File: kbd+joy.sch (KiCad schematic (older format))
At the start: 50 parts, among them CN2 KEYBOARD_HEADER, CN4 JOY1, CN5 JOY2, U11 74LS125, U13 MOS_6529

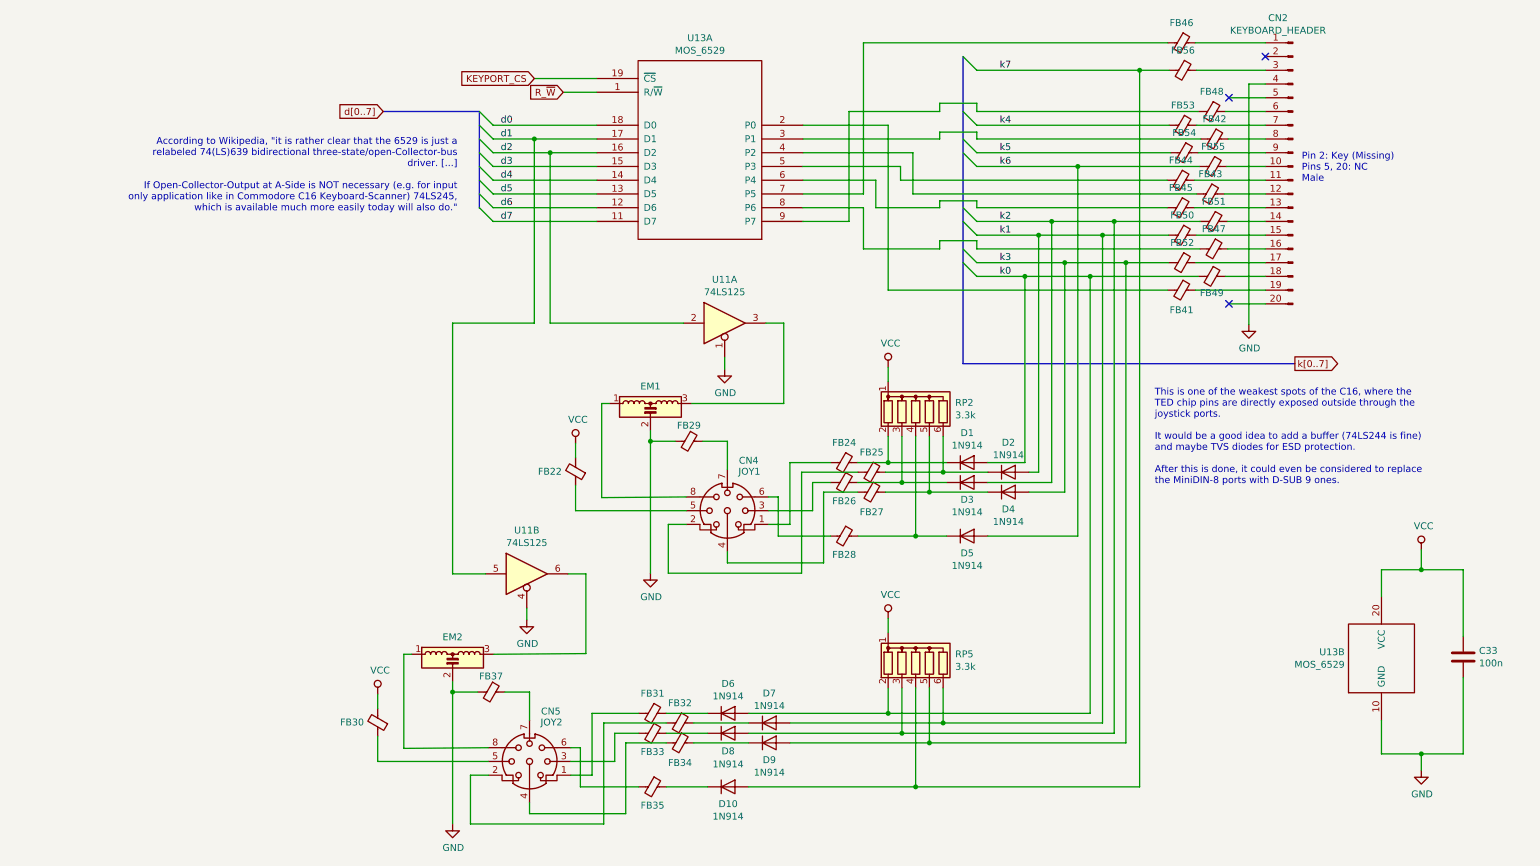
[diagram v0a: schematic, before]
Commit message: Map RP3/4 and add (J)D1/2
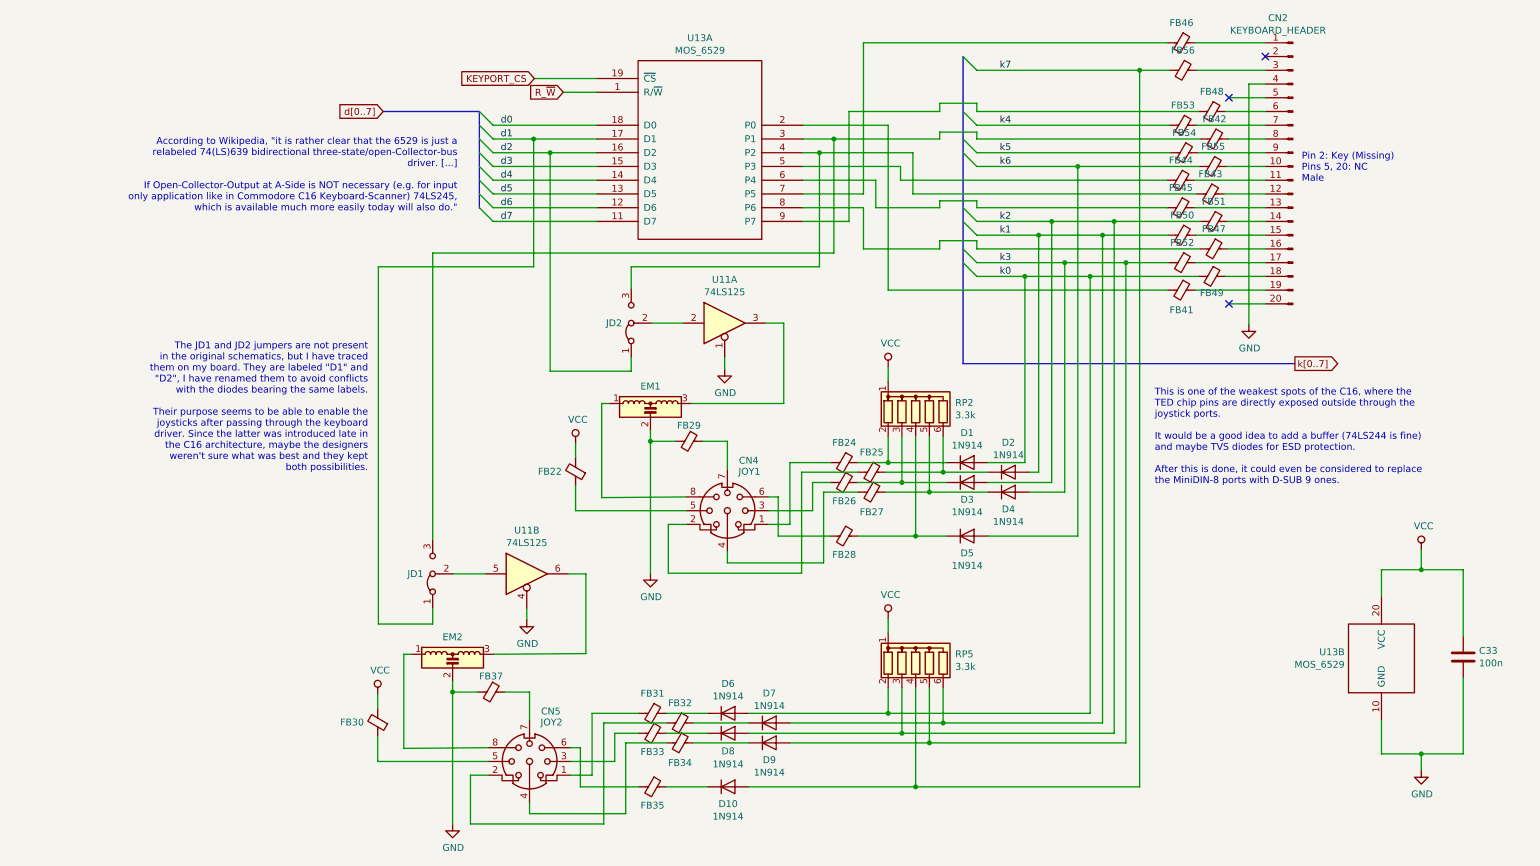
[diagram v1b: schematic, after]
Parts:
- added JD1, JD2: Jumper_3_Bridged12, LittleSixteen:SolderJumper2x, symbol Jumper:Jumper_3_Bridged12
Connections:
- net d1: now also JD1.1 (A); no longer U11.5
- net d2: now also JD2.1 (A); no longer U11.2
- net at FB42.2, U13.3 (P1): now also JD1.3 (B)
- net at FB43.2, U13.4 (P2): now also JD2.3 (B)
- new net: JD2.2 (C), U11.2
- new net: JD1.2 (C), U11.5
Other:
- note added: "The JD1 and JD2 jumpers are not present\nin the original schematics, but I have traced\nthem on my board. They are labeled "D1" and\n"D2", I have renamed them to avoid conflicts\nwith the diodes bearing the same labels.\n\nTheir purpose seems to be able to enable the\njoysticks after passing through the keyboard\ndriver. Since the latter was introduced late in\nthe C16 architecture, maybe the des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"
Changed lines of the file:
@@
 Sheet 6 11
 Title "LittleSixteen"
-Date "2020-01-03"
+Date "2020-01-20"
 Rev "1git"
 Comp "SukkoPera"
@@
 	6485 1480 6485 2680
 Wire Wire Line
-	5865 1680 6665 1680
+	5865 1680 5985 1680
 Wire Wire Line
 	6665 1680 6665 1980
@@
 	7030 1580 7130 1680
 Wire Wire Line
-	5865 1580 6860 1580
+	5865 1580 6090 1580
 Wire Wire Line
 	6860 1580 6860 1530
@@
 	4365 1480 3610 1480
 Wire Wire Line
-	4365 1580 3910 1580
+	4365 1580 3905 1580
 Wire Wire Line
 	4365 1680 4025 1680
@@
 Wire Wire Line
 	5295 3255 5295 3170
-Wire Wire Line
-	4025 1680 4025 2920
-Wire Wire Line
-	4025 2920 4995 2920
 Connection ~ 4025 1680
 Wire Wire Line
@@
 $EndComp
 Wire Wire Line
-	3910 1580 3910 2920
-Wire Wire Line
-	3910 2920 3315 2920
-Wire Wire Line
-	3315 2920 3315 4745
-Connection ~ 3910 1580
-Wire Wire Line
-	3910 1580 3610 1580
-Wire Wire Line
-	3315 4745 3555 4745
+	3905 1580 3905 2510
+Connection ~ 3905 1580
+Wire Wire Line
+	3905 1580 3610 1580
 Wire Wire Line
 	7955 5760 7955 2580
@@
 Wire Wire Line
 	6685 6295 8315 6295
+Wire Wire Line
+	4765 2920 4995 2920
+Wire Wire Line
+	3905 2510 2775 2510
+Wire Wire Line
+	4025 3270 4615 3270
+Wire Wire Line
+	4615 3270 4615 3170
+Wire Wire Line
+	4025 1680 4025 3270
+Wire Wire Line
+	5985 1680 5985 2510
+Wire Wire Line
+	5985 2510 4615 2510
+Wire Wire Line
+	4615 2510 4615 2670
+Connection ~ 5985 1680
+Wire Wire Line
+	5985 1680 6665 1680
+Wire Wire Line
+	6090 1580 6090 2410
+Connection ~ 6090 1580
+Wire Wire Line
+	6090 1580 6860 1580
+Wire Wire Line
+	3320 4745 3555 4745
+Wire Wire Line
+	2775 5110 3170 5110
+Wire Wire Line
+	3170 5110 3170 4995
+Wire Wire Line
+	2775 2510 2775 5110
+Wire Wire Line
+	6090 2410 3170 2410
+Wire Wire Line
+	3170 2410 3170 4495
+Text Notes 2700 4005 2    50   ~ 0
+The JD1 and JD2 jumpers are not present\nin the original schematics, but I have traced\nthem on my board. They are labeled "D1" and\n"D2", I have renamed them to avoid conflicts\nwith the diodes bearing the same labels.\n\nTheir purpose seems to be able to enable the\njoysticks after passing through the keyboard\ndriver. Since the latter was introduced late in\nthe C16 architecture, maybe the designers\nweren't sure what was best and they kept \nboth possibilities.
+$Comp
+L Jumper:Jumper_3_Bridged12 JD2
+U 1 1 5E31F2CA
+P 4615 2920
+F 0 "JD2" V 4615 2987 50  0000 L CNN
+F 1 "Jumper_3_Bridged12" V 4660 2987 50  0001 L CNN
+F 2 "LittleSixteen:SolderJumper2x" H 4615 2920 50  0001 C CNN
+F 3 "~" H 4615 2920 50  0001 C CNN
+	1    4615 2920
+	0    -1   -1   0
+$EndComp
+$Comp
+L Jumper:Jumper_3_Bridged12 JD1
+U 1 1 5E450B9C
+P 3170 4745
+F 0 "JD1" V 3170 4812 50  0000 L CNN
+F 1 "Jumper_3_Bridged12" V 3215 4812 50  0001 L CNN
+F 2 "LittleSixteen:SolderJumper2x" H 3170 4745 50  0001 C CNN
+F 3 "~" H 3170 4745 50  0001 C CNN
+	1    3170 4745
+	0    -1   -1   0
+$EndComp
 Wire Bus Line
 	3510 1380 3510 2085

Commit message: Add pin headers
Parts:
- CN2: footprint (none) -> Connector_PinHeader_2.54mm:PinHeader_1x20_P2.54mm_Vertical
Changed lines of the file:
@@
 F 0 "CN2" H 9538 2861 50  0000 C CNN
 F 1 "KEYBOARD_HEADER" H 9538 2770 50  0000 C CNN
-F 2 "" H 9430 1780 50  0001 C CNN
+F 2 "Connector_PinHeader_2.54mm:PinHeader_1x20_P2.54mm_Vertical" H 9430 1780 50  0001 C CNN
 F 3 "~" H 9430 1780 50  0001 C CNN
 	1    9430 1780

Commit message: Add ceramics
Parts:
- C33: footprint (none) -> Capacitor_THT:C_Disc_D8.0mm_W2.5mm_P5.00mm
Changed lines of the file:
@@
 F 0 "C33" H 10785 5396 50  0000 L CNN
 F 1 "100n" H 10785 5305 50  0000 L CNN
-F 2 "" H 10708 5200 50  0001 C CNN
+F 2 "Capacitor_THT:C_Disc_D8.0mm_W2.5mm_P5.00mm" H 10708 5200 50  0001 C CNN
 F 3 "~" H 10670 5350 50  0001 C CNN
 	1    10670 5350

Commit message: Add diodes
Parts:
- D1, D10, D2, D3, D4, D5, D6, D7, D8, D9: footprint Diode_THT:D_DO-35_SOD27_P7.62mm_Horizontal -> Diode_THT:D_DO-35_SOD27_P5.08mm_Vertical_KathodeUp
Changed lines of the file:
@@
 F 0 "D1" H 7060 4151 50  0000 C CNN
 F 1 "1N914" H 7060 4060 50  0000 C CNN
-F 2 "Diode_THT:D_DO-35_SOD27_P7.62mm_Horizontal" H 7060 3760 50  0001 C CNN
+F 2 "Diode_THT:D_DO-35_SOD27_P5.08mm_Vertical_KathodeUp" H 7060 3760 50  0001 C CNN
 F 3 "http://www.vishay.com/docs/85622/1n914.pdf" H 7060 3935 50  0001 C CNN
 	1    7060 3935
@@
 F 0 "D2" H 7360 4221 50  0000 C CNN
 F 1 "1N914" H 7360 4130 50  0000 C CNN
-F 2 "Diode_THT:D_DO-35_SOD27_P7.62mm_Horizontal" H 7360 3830 50  0001 C CNN
+F 2 "Diode_THT:D_DO-35_SOD27_P5.08mm_Vertical_KathodeUp" H 7360 3830 50  0001 C CNN
 F 3 "http://www.vishay.com/docs/85622/1n914.pdf" H 7360 4005 50  0001 C CNN
 	1    7360 4005
@@
 F 0 "D3" H 7060 3956 50  0000 C CNN
 F 1 "1N914" H 7060 3865 50  0000 C CNN
-F 2 "Diode_THT:D_DO-35_SOD27_P7.62mm_Horizontal" H 7060 3905 50  0001 C CNN
+F 2 "Diode_THT:D_DO-35_SOD27_P5.08mm_Vertical_KathodeUp" H 7060 3905 50  0001 C CNN
 F 3 "http://www.vishay.com/docs/85622/1n914.pdf" H 7060 4080 50  0001 C CNN
 	1    7060 4080
@@
 F 0 "D4" H 7360 4026 50  0000 C CNN
 F 1 "1N914" H 7360 3935 50  0000 C CNN
-F 2 "Diode_THT:D_DO-35_SOD27_P7.62mm_Horizontal" H 7360 3975 50  0001 C CNN
+F 2 "Diode_THT:D_DO-35_SOD27_P5.08mm_Vertical_KathodeUp" H 7360 3975 50  0001 C CNN
 F 3 "http://www.vishay.com/docs/85622/1n914.pdf" H 7360 4150 50  0001 C CNN
 	1    7360 4150
@@
 F 0 "D5" H 7060 4346 50  0000 C CNN
 F 1 "1N914" H 7060 4255 50  0000 C CNN
-F 2 "Diode_THT:D_DO-35_SOD27_P7.62mm_Horizontal" H 7060 4295 50  0001 C CNN
+F 2 "Diode_THT:D_DO-35_SOD27_P5.08mm_Vertical_KathodeUp" H 7060 4295 50  0001 C CNN
 F 3 "http://www.vishay.com/docs/85622/1n914.pdf" H 7060 4470 50  0001 C CNN
 	1    7060 4470
@@
 F 0 "D6" H 5320 5976 50  0000 C CNN
 F 1 "1N914" H 5320 5885 50  0000 C CNN
-F 2 "Diode_THT:D_DO-35_SOD27_P7.62mm_Horizontal" H 5320 5585 50  0001 C CNN
+F 2 "Diode_THT:D_DO-35_SOD27_P5.08mm_Vertical_KathodeUp" H 5320 5585 50  0001 C CNN
 F 3 "http://www.vishay.com/docs/85622/1n914.pdf" H 5320 5760 50  0001 C CNN
 	1    5320 5760
@@
 F 0 "D7" H 5620 6046 50  0000 C CNN
 F 1 "1N914" H 5620 5955 50  0000 C CNN
-F 2 "Diode_THT:D_DO-35_SOD27_P7.62mm_Horizontal" H 5620 5655 50  0001 C CNN
+F 2 "Diode_THT:D_DO-35_SOD27_P5.08mm_Vertical_KathodeUp" H 5620 5655 50  0001 C CNN
 F 3 "http://www.vishay.com/docs/85622/1n914.pdf" H 5620 5830 50  0001 C CNN
 	1    5620 5830
@@
 F 0 "D8" H 5320 5775 50  0000 C CNN
 F 1 "1N914" H 5320 5680 50  0000 C CNN
-F 2 "Diode_THT:D_DO-35_SOD27_P7.62mm_Horizontal" H 5320 5730 50  0001 C CNN
+F 2 "Diode_THT:D_DO-35_SOD27_P5.08mm_Vertical_KathodeUp" H 5320 5730 50  0001 C CNN
 F 3 "http://www.vishay.com/docs/85622/1n914.pdf" H 5320 5905 50  0001 C CNN
 	1    5320 5905
@@
 F 0 "D9" H 5620 5851 50  0000 C CNN
 F 1 "1N914" H 5620 5760 50  0000 C CNN
-F 2 "Diode_THT:D_DO-35_SOD27_P7.62mm_Horizontal" H 5620 5800 50  0001 C CNN
+F 2 "Diode_THT:D_DO-35_SOD27_P5.08mm_Vertical_KathodeUp" H 5620 5800 50  0001 C CNN
 F 3 "http://www.vishay.com/docs/85622/1n914.pdf" H 5620 5975 50  0001 C CNN
 	1    5620 5975
@@
 F 0 "D10" H 5320 6171 50  0000 C CNN
 F 1 "1N914" H 5320 6080 50  0000 C CNN
-F 2 "Diode_THT:D_DO-35_SOD27_P7.62mm_Horizontal" H 5320 6120 50  0001 C CNN
+F 2 "Diode_THT:D_DO-35_SOD27_P5.08mm_Vertical_KathodeUp" H 5320 6120 50  0001 C CNN
 F 3 "http://www.vishay.com/docs/85622/1n914.pdf" H 5320 6295 50  0001 C CNN
 	1    5320 6295

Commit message: Add crystal
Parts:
- EM1, EM2: footprint (none) -> CSeventeen:EMI_Filter
- FB22, FB24, FB25, FB26, FB27, FB28, FB29, FB30, FB31, FB32, FB33, FB34, FB35, FB37, FB41, FB42, FB43, FB44, FB45, FB46, FB47, FB48, FB49, FB50, FB51, FB52, FB53, FB54, FB55, FB56: footprint (none) -> CSeventeen:Ferrite
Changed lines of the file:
@@
 F 0 "EM1" H 4755 3830 50  0000 C CNN
 F 1 "EMI_Filter_LCL" H 4755 3831 50  0001 C CNN
-F 2 "" V 4755 3605 50  0001 C CNN
+F 2 "CSeventeen:EMI_Filter" V 4755 3605 50  0001 C CNN
 F 3 "http://www.murata.com/~/media/webrenewal/support/library/catalog/products/emc/emifil/c31e.ashx?la=en-gb" V 4755 3605 50  0001 C CNN
 	1    4755 3605
@@
 F 0 "FB24" V 6020 3935 50  0000 C CNN
 F 1 "Ferrite_Bead_Small" V 6019 3935 50  0001 C CNN
-F 2 "" V 6095 3935 50  0001 C CNN
+F 2 "CSeventeen:Ferrite" V 6095 3935 50  0001 C CNN
 F 3 "~" H 6165 3935 50  0001 C CNN
 	1    6165 3935
@@
 F 0 "FB25" V 6220 4005 50  0000 C CNN
 F 1 "Ferrite_Bead_Small" V 6219 4005 50  0001 C CNN
-F 2 "" V 6295 4005 50  0001 C CNN
+F 2 "CSeventeen:Ferrite" V 6295 4005 50  0001 C CNN
 F 3 "~" H 6365 4005 50  0001 C CNN
 	1    6365 4005
@@
 F 0 "FB27" V 6510 4150 50  0000 C CNN
 F 1 "Ferrite_Bead_Small" V 6219 4150 50  0001 C CNN
-F 2 "" V 6295 4150 50  0001 C CNN
+F 2 "CSeventeen:Ferrite" V 6295 4150 50  0001 C CNN
 F 3 "~" H 6365 4150 50  0001 C CNN
 	1    6365 4150
@@
 F 0 "FB26" V 6300 4080 50  0000 C CNN
 F 1 "Ferrite_Bead_Small" V 6019 4080 50  0001 C CNN
-F 2 "" V 6095 4080 50  0001 C CNN
+F 2 "CSeventeen:Ferrite" V 6095 4080 50  0001 C CNN
 F 3 "~" H 6165 4080 50  0001 C CNN
 	1    6165 4080
@@
 F 0 "FB22" H 4310 4000 50  0000 L CNN
 F 1 "Ferrite_Bead_Small" V 4064 4000 50  0001 C CNN
-F 2 "" V 4140 4000 50  0001 C CNN
+F 2 "CSeventeen:Ferrite" V 4140 4000 50  0001 C CNN
 F 3 "~" H 4210 4000 50  0001 C CNN
 	1    4210 4000
@@
 F 0 "FB28" V 6300 4470 50  0000 C CNN
 F 1 "Ferrite_Bead_Small" V 6019 4470 50  0001 C CNN
-F 2 "" V 6095 4470 50  0001 C CNN
+F 2 "CSeventeen:Ferrite" V 6095 4470 50  0001 C CNN
 F 3 "~" H 6165 4470 50  0001 C CNN
 	1    6165 4470
@@
 F 0 "FB29" V 4920 3780 50  0000 C CNN
 F 1 "Ferrite_Bead_Small" V 4889 3780 50  0001 C CNN
-F 2 "" V 4965 3780 50  0001 C CNN
+F 2 "CSeventeen:Ferrite" V 4965 3780 50  0001 C CNN
 F 3 "~" H 5035 3780 50  0001 C CNN
 	1    5035 3780
@@
 F 0 "EM2" H 3315 5655 50  0000 C CNN
 F 1 "EMI_Filter_LCL" H 3315 5656 50  0001 C CNN
-F 2 "" V 3315 5430 50  0001 C CNN
+F 2 "CSeventeen:EMI_Filter" V 3315 5430 50  0001 C CNN
 F 3 "http://www.murata.com/~/media/webrenewal/support/library/catalog/products/emc/emifil/c31e.ashx?la=en-gb" V 3315 5430 50  0001 C CNN
 	1    3315 5430
@@
 F 0 "FB31" V 4625 5760 50  0000 C CNN
 F 1 "Ferrite_Bead_Small" V 4624 5760 50  0001 C CNN
-F 2 "" V 4700 5760 50  0001 C CNN
+F 2 "CSeventeen:Ferrite" V 4700 5760 50  0001 C CNN
 F 3 "~" H 4770 5760 50  0001 C CNN
 	1    4770 5760
@@
 F 0 "FB32" V 4825 5830 50  0000 C CNN
 F 1 "Ferrite_Bead_Small" V 4824 5830 50  0001 C CNN
-F 2 "" V 4900 5830 50  0001 C CNN
+F 2 "CSeventeen:Ferrite" V 4900 5830 50  0001 C CNN
 F 3 "~" H 4970 5830 50  0001 C CNN
 	1    4970 5830
@@
 F 0 "FB34" V 5115 5975 50  0000 C CNN
 F 1 "Ferrite_Bead_Small" V 4824 5975 50  0001 C CNN
-F 2 "" V 4900 5975 50  0001 C CNN
+F 2 "CSeventeen:Ferrite" V 4900 5975 50  0001 C CNN
 F 3 "~" H 4970 5975 50  0001 C CNN
 	1    4970 5975
@@
 F 0 "FB33" V 4905 5905 50  0000 C CNN
 F 1 "Ferrite_Bead_Small" V 4624 5905 50  0001 C CNN
-F 2 "" V 4700 5905 50  0001 C CNN
+F 2 "CSeventeen:Ferrite" V 4700 5905 50  0001 C CNN
 F 3 "~" H 4770 5905 50  0001 C CNN
 	1    4770 5905
@@
 F 0 "FB30" H 2870 5825 50  0000 L CNN
 F 1 "Ferrite_Bead_Small" V 2624 5825 50  0001 C CNN
-F 2 "" V 2700 5825 50  0001 C CNN
+F 2 "CSeventeen:Ferrite" V 2700 5825 50  0001 C CNN
 F 3 "~" H 2770 5825 50  0001 C CNN
 	1    2770 5825
@@
 F 0 "FB35" V 4905 6295 50  0000 C CNN
 F 1 "Ferrite_Bead_Small" V 4624 6295 50  0001 C CNN
-F 2 "" V 4700 6295 50  0001 C CNN
+F 2 "CSeventeen:Ferrite" V 4700 6295 50  0001 C CNN
 F 3 "~" H 4770 6295 50  0001 C CNN
 	1    4770 6295
@@
 F 0 "FB37" V 3480 5605 50  0000 C CNN
 F 1 "Ferrite_Bead_Small" V 3449 5605 50  0001 C CNN
-F 2 "" V 3525 5605 50  0001 C CNN
+F 2 "CSeventeen:Ferrite" V 3525 5605 50  0001 C CNN
 F 3 "~" H 3595 5605 50  0001 C CNN
 	1    3595 5605
@@
 F 0 "FB46" V 8475 880 50  0000 C CNN
 F 1 "Ferrite_Bead_Small" V 8474 880 50  0001 C CNN
-F 2 "" V 8550 880 50  0001 C CNN
+F 2 "CSeventeen:Ferrite" V 8550 880 50  0001 C CNN
 F 3 "~" H 8620 880 50  0001 C CNN
 	1    8620 880
@@
 F 0 "FB56" V 8485 1080 50  0000 C CNN
 F 1 "Ferrite_Bead_Small" V 8484 1080 50  0001 C CNN
-F 2 "" V 8560 1080 50  0001 C CNN
+F 2 "CSeventeen:Ferrite" V 8560 1080 50  0001 C CNN
 F 3 "~" H 8630 1080 50  0001 C CNN
 	1    8630 1080
@@
 F 0 "FB53" V 8485 1480 50  0000 C CNN
 F 1 "Ferrite_Bead_Small" V 8484 1480 50  0001 C CNN
-F 2 "" V 8560 1480 50  0001 C CNN
+F 2 "CSeventeen:Ferrite" V 8560 1480 50  0001 C CNN
 F 3 "~" H 8630 1480 50  0001 C CNN
 	1    8630 1480
@@
 F 0 "FB54" V 8495 1680 50  0000 C CNN
 F 1 "Ferrite_Bead_Small" V 8494 1680 50  0001 C CNN
-F 2 "" V 8570 1680 50  0001 C CNN
+F 2 "CSeventeen:Ferrite" V 8570 1680 50  0001 C CNN
 F 3 "~" H 8640 1680 50  0001 C CNN
 	1    8640 1680
@@
 F 0 "FB44" V 8470 1880 50  0000 C CNN
 F 1 "Ferrite_Bead_Small" V 8469 1880 50  0001 C CNN
-F 2 "" V 8545 1880 50  0001 C CNN
+F 2 "CSeventeen:Ferrite" V 8545 1880 50  0001 C CNN
 F 3 "~" H 8615 1880 50  0001 C CNN
 	1    8615 1880
@@
 F 0 "FB45" V 8470 2080 50  0000 C CNN
 F 1 "Ferrite_Bead_Small" V 8469 2080 50  0001 C CNN
-F 2 "" V 8545 2080 50  0001 C CNN
+F 2 "CSeventeen:Ferrite" V 8545 2080 50  0001 C CNN
 F 3 "~" H 8615 2080 50  0001 C CNN
 	1    8615 2080
@@
 F 0 "FB50" V 8480 2280 50  0000 C CNN
 F 1 "Ferrite_Bead_Small" V 8479 2280 50  0001 C CNN
-F 2 "" V 8555 2280 50  0001 C CNN
+F 2 "CSeventeen:Ferrite" V 8555 2280 50  0001 C CNN
 F 3 "~" H 8625 2280 50  0001 C CNN
 	1    8625 2280
@@
 F 0 "FB52" V 8480 2480 50  0000 C CNN
 F 1 "Ferrite_Bead_Small" V 8479 2480 50  0001 C CNN
-F 2 "" V 8555 2480 50  0001 C CNN
+F 2 "CSeventeen:Ferrite" V 8555 2480 50  0001 C CNN
 F 3 "~" H 8625 2480 50  0001 C CNN
 	1    8625 2480
@@
 F 0 "FB41" V 8765 2680 50  0000 C CNN
 F 1 "Ferrite_Bead_Small" V 8474 2680 50  0001 C CNN
-F 2 "" V 8550 2680 50  0001 C CNN
+F 2 "CSeventeen:Ferrite" V 8550 2680 50  0001 C CNN
 F 3 "~" H 8620 2680 50  0001 C CNN
 	1    8620 2680
@@
 F 0 "FB48" V 8695 1380 50  0000 C CNN
 F 1 "Ferrite_Bead_Small" V 8694 1380 50  0001 C CNN
-F 2 "" V 8770 1380 50  0001 C CNN
+F 2 "CSeventeen:Ferrite" V 8770 1380 50  0001 C CNN
 F 3 "~" H 8840 1380 50  0001 C CNN
 	1    8840 1380
@@
 F 0 "FB42" V 8715 1580 50  0000 C CNN
 F 1 "Ferrite_Bead_Small" V 8714 1580 50  0001 C CNN
-F 2 "" V 8790 1580 50  0001 C CNN
+F 2 "CSeventeen:Ferrite" V 8790 1580 50  0001 C CNN
 F 3 "~" H 8860 1580 50  0001 C CNN
 	1    8860 1580
@@
 F 0 "FB55" V 8705 1780 50  0000 C CNN
 F 1 "Ferrite_Bead_Small" V 8704 1780 50  0001 C CNN
-F 2 "" V 8780 1780 50  0001 C CNN
+F 2 "CSeventeen:Ferrite" V 8780 1780 50  0001 C CNN
 F 3 "~" H 8850 1780 50  0001 C CNN
 	1    8850 1780
@@
 F 0 "FB43" V 8685 1980 50  0000 C CNN
 F 1 "Ferrite_Bead_Small" V 8684 1980 50  0001 C CNN
-F 2 "" V 8760 1980 50  0001 C CNN
+F 2 "CSeventeen:Ferrite" V 8760 1980 50  0001 C CNN
 F 3 "~" H 8830 1980 50  0001 C CNN
 	1    8830 1980
@@
 F 0 "FB51" V 8710 2180 50  0000 C CNN
 F 1 "Ferrite_Bead_Small" V 8709 2180 50  0001 C CNN
-F 2 "" V 8785 2180 50  0001 C CNN
+F 2 "CSeventeen:Ferrite" V 8785 2180 50  0001 C CNN
 F 3 "~" H 8855 2180 50  0001 C CNN
 	1    8855 2180
@@
 F 0 "FB47" V 8710 2380 50  0000 C CNN
 F 1 "Ferrite_Bead_Small" V 8709 2380 50  0001 C CNN
-F 2 "" V 8785 2380 50  0001 C CNN
+F 2 "CSeventeen:Ferrite" V 8785 2380 50  0001 C CNN
 F 3 "~" H 8855 2380 50  0001 C CNN
 	1    8855 2380
@@
 F 0 "FB49" V 8960 2580 50  0000 C CNN
 F 1 "Ferrite_Bead_Small" V 8694 2580 50  0001 C CNN
-F 2 "" V 8770 2580 50  0001 C CNN
+F 2 "CSeventeen:Ferrite" V 8770 2580 50  0001 C CNN
 F 3 "~" H 8840 2580 50  0001 C CNN
 	1    8840 2580

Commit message: Use 3d models from github.com/StormTrooper/Commodore-Plus4
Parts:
- CN4, CN5: footprint (none) -> CommodorePlus4:Connector_Mini-DIN_Female_8Pin_2rows
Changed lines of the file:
@@
 F 0 "CN4" H 5470 4650 50  0000 C CNN
 F 1 "JOY1" H 5475 4570 50  0000 C CNN
-F 2 "" V 5305 4275 50  0001 C CNN
+F 2 "CommodorePlus4:Connector_Mini-DIN_Female_8Pin_2rows" V 5305 4275 50  0001 C CNN
 F 3 "http://service.powerdynamics.com/ec/Catalog17/Section%2011.pdf" V 5305 4275 50  0001 C CNN
 	1    5315 4285
@@
 F 0 "CN5" H 4030 6475 50  0000 C CNN
 F 1 "JOY2" H 4035 6395 50  0000 C CNN
-F 2 "" V 3865 6100 50  0001 C CNN
+F 2 "CommodorePlus4:Connector_Mini-DIN_Female_8Pin_2rows" V 3865 6100 50  0001 C CNN
 F 3 "http://service.powerdynamics.com/ec/Catalog17/Section%2011.pdf" V 3865 6100 50  0001 C CNN
 	1    3875 6110
